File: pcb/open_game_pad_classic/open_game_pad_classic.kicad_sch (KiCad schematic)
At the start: 54 parts, among them J1 COM-09032, J2 COM-09032

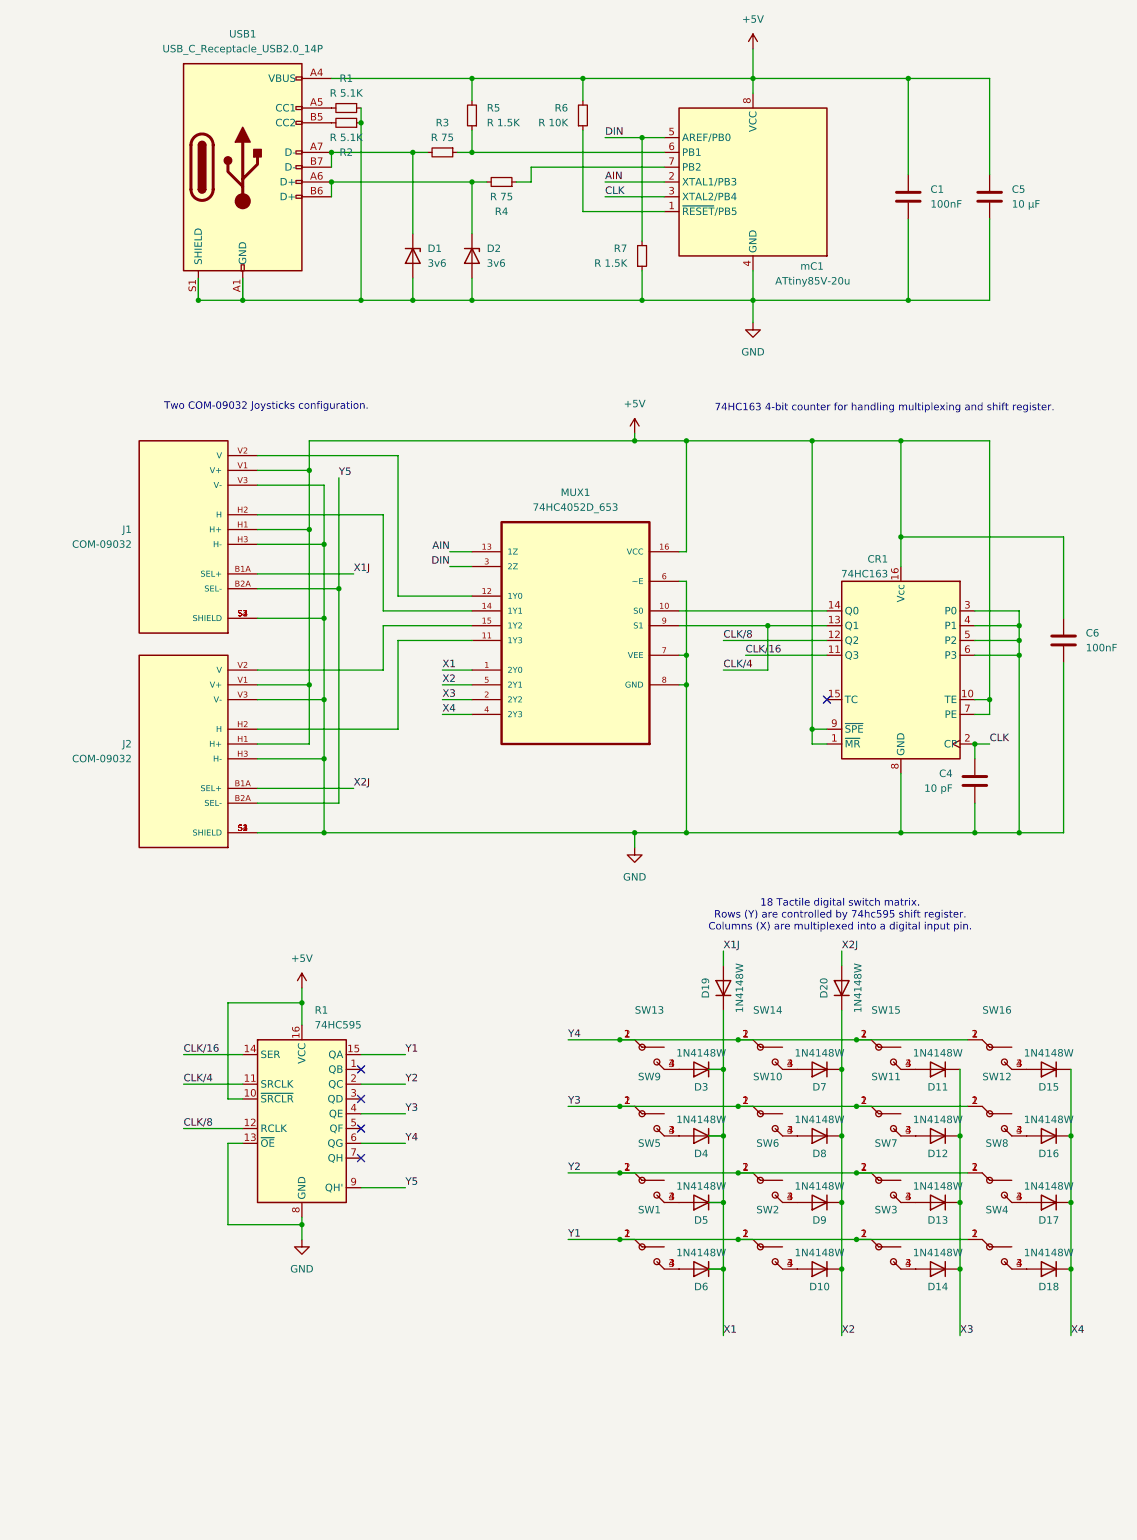
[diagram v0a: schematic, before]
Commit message: Imported footprints.
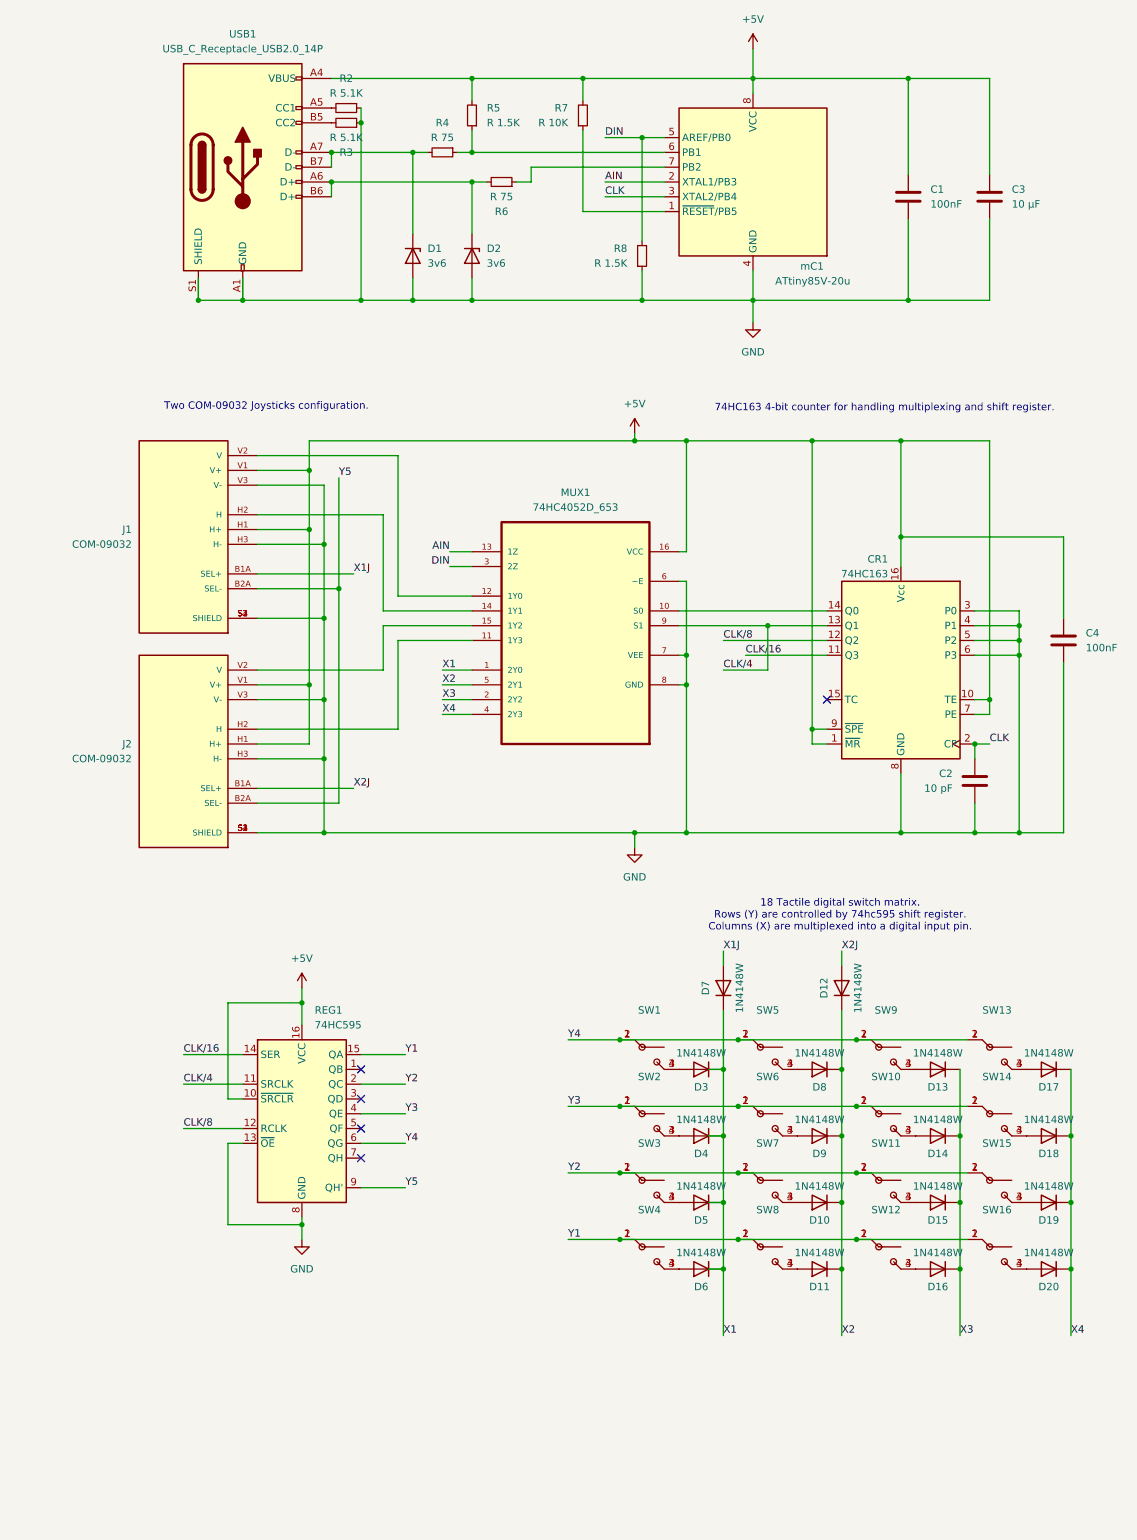
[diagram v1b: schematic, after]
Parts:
- CR1: footprint Package_SO:SOIC-16W_7.5x10.3mm_P1.27mm -> SN74HC163DR:SOIC127P600X175-16N
- REG1: renamed from R1; footprint (none) -> 74HC595DR:SOIC127P600X175-16N
- SW1: renamed from SW13; footprint TS02-66-95-BK-260-LCR-D:SW_TS02-66-95-BK-260-LCR-D -> TS04-66-95-BK-100-SMT:SW_TS04-66-95-BK-100-SMT
- SW10: renamed from SW11; footprint TS02-66-95-BK-260-LCR-D:SW_TS02-66-95-BK-260-LCR-D -> TS04-66-95-BK-100-SMT:SW_TS04-66-95-BK-100-SMT
- SW11: renamed from SW7; footprint TS02-66-95-BK-260-LCR-D:SW_TS02-66-95-BK-260-LCR-D -> TS04-66-95-BK-100-SMT:SW_TS04-66-95-BK-100-SMT
- SW12: renamed from SW3; footprint TS02-66-95-BK-260-LCR-D:SW_TS02-66-95-BK-260-LCR-D -> TS04-66-95-BK-100-SMT:SW_TS04-66-95-BK-100-SMT
- SW13: renamed from SW16; footprint TS02-66-95-BK-260-LCR-D:SW_TS02-66-95-BK-260-LCR-D -> TS04-66-95-BK-100-SMT:SW_TS04-66-95-BK-100-SMT
- SW14: renamed from SW12; footprint TS02-66-95-BK-260-LCR-D:SW_TS02-66-95-BK-260-LCR-D -> TS04-66-95-BK-100-SMT:SW_TS04-66-95-BK-100-SMT
- SW15: renamed from SW8; footprint TS02-66-95-BK-260-LCR-D:SW_TS02-66-95-BK-260-LCR-D -> TS04-66-95-BK-100-SMT:SW_TS04-66-95-BK-100-SMT
- SW16: renamed from SW4; footprint TS02-66-95-BK-260-LCR-D:SW_TS02-66-95-BK-260-LCR-D -> TS04-66-95-BK-100-SMT:SW_TS04-66-95-BK-100-SMT
- SW2: renamed from SW9; footprint TS02-66-95-BK-260-LCR-D:SW_TS02-66-95-BK-260-LCR-D -> TS04-66-95-BK-100-SMT:SW_TS04-66-95-BK-100-SMT
- SW3: renamed from SW5; footprint TS02-66-95-BK-260-LCR-D:SW_TS02-66-95-BK-260-LCR-D -> TS04-66-95-BK-100-SMT:SW_TS04-66-95-BK-100-SMT
- SW4: renamed from SW1; footprint TS02-66-95-BK-260-LCR-D:SW_TS02-66-95-BK-260-LCR-D -> TS04-66-95-BK-100-SMT:SW_TS04-66-95-BK-100-SMT
- SW5: renamed from SW14; footprint TS02-66-95-BK-260-LCR-D:SW_TS02-66-95-BK-260-LCR-D -> TS04-66-95-BK-100-SMT:SW_TS04-66-95-BK-100-SMT
- SW6: renamed from SW10; footprint TS02-66-95-BK-260-LCR-D:SW_TS02-66-95-BK-260-LCR-D -> TS04-66-95-BK-100-SMT:SW_TS04-66-95-BK-100-SMT
- SW7: renamed from SW6; footprint TS02-66-95-BK-260-LCR-D:SW_TS02-66-95-BK-260-LCR-D -> TS04-66-95-BK-100-SMT:SW_TS04-66-95-BK-100-SMT
- SW8: renamed from SW2; footprint TS02-66-95-BK-260-LCR-D:SW_TS02-66-95-BK-260-LCR-D -> TS04-66-95-BK-100-SMT:SW_TS04-66-95-BK-100-SMT
- SW9: renamed from SW15; footprint TS02-66-95-BK-260-LCR-D:SW_TS02-66-95-BK-260-LCR-D -> TS04-66-95-BK-100-SMT:SW_TS04-66-95-BK-100-SMT
- mC1: footprint Package_SO:SOIC-8W_5.3x5.3mm_P1.27mm -> ATTINY85-20SU:SOIC127P798X216-8N
- renumbered C4 to C2, C5 to C3, C6 to C4, D9 to D10, D10 to D11, D20 to D12, D11 to D13, D12 to D14, D13 to D15, D14 to D16, D15 to D17, D16 to D18, D17 to D19, D18 to D20, D19 to D7, D7 to D8, D8 to D9, R1 to R2, R2 to R3, R3 to R4, R4 to R6, R6 to R7, R7 to R8

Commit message: Updated the PCB based on the new schematic design.
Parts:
- C2, C4: footprint Capacitor_SMD:C_0201_0603Metric -> Capacitor_SMD:C_0402_1005Metric
- R7: footprint Resistor_SMD:R_0402_1005Metric -> Resistor_SMD:R_0603_1608Metric
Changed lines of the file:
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@@
 			)
 		)
-		(property "Footprint" "Capacitor_SMD:C_0201_0603Metric"
+		(property "Footprint" "Capacitor_SMD:C_0402_1005Metric"
 			(at 187.6552 130.81 0)
 			(effects
@@
 			)
 		)
-		(property "Footprint" "Resistor_SMD:R_0402_1005Metric"
+		(property "Footprint" "Resistor_SMD:R_0603_1608Metric"
 			(at 104.14 36.83 0)
 			(effects
@@
 			)
 		)
-		(property "Footprint" "Capacitor_SMD:C_0201_0603Metric"
+		(property "Footprint" "Capacitor_SMD:C_0402_1005Metric"
 			(at 170.4848 154.94 0)
 			(effects

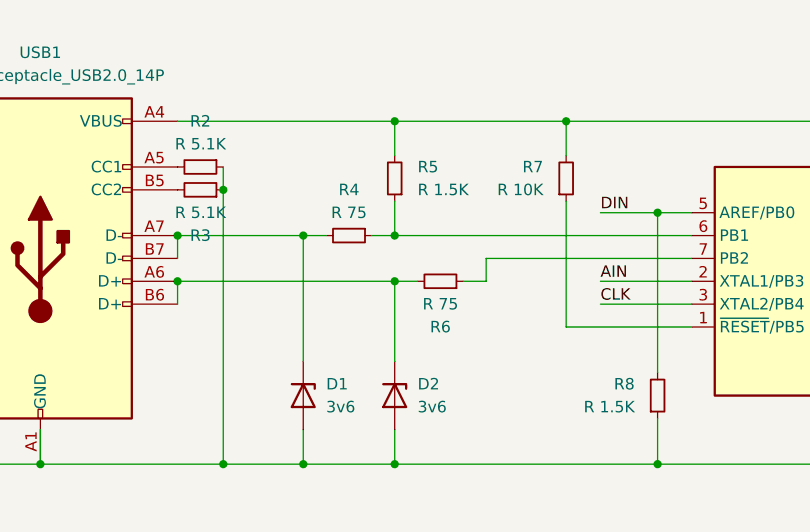
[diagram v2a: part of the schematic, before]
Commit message: Deleted uneccessary files.
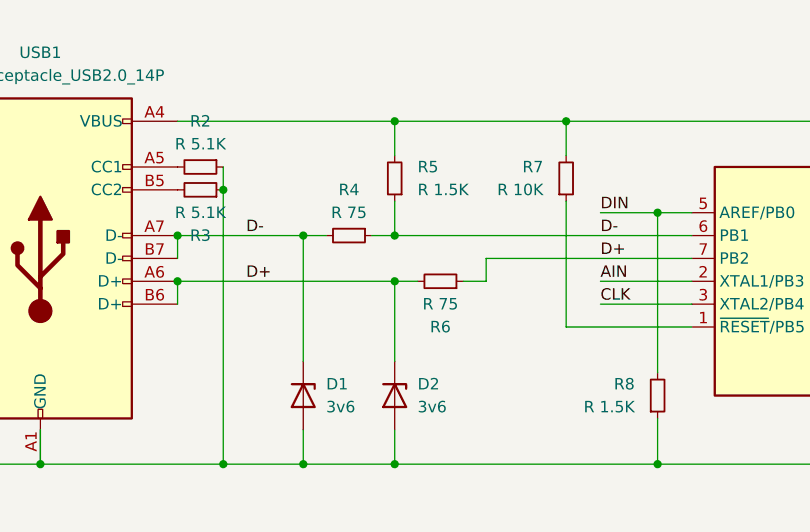
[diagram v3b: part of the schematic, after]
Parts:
- C1, C3: footprint Capacitor_SMD:C_0603_1608Metric -> Capacitor_SMD:C_0402_1005Metric
- D1: footprint Diode_SMD:D_MiniMELF -> Diode_SMD:D_0201_0603Metric
- D2: footprint Diode_SMD:D_MiniMELF -> Diode_SMD:D_0603_1608Metric
- R4, R6: footprint Resistor_SMD:R_0402_1005Metric -> Resistor_SMD:R_0201_0603Metric
- R5: footprint Resistor_SMD:R_0603_1608Metric -> Resistor_SMD:R_0201_0603Metric
- R7, R8: footprint Resistor_SMD:R_0603_1608Metric -> Resistor_SMD:R_0402_1005Metric
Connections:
- net D-: now reaches R4.1, R5.1, mC1.6 (PB1)
- net D-: now also D1.1 (K), R4.2, USB1.A7 (D-), USB1.B7 (D-)
- net D+: now reaches R6.1, mC1.7 (PB2)
- net D+: now also D2.1 (K), R6.2, USB1.A6 (D+), USB1.B6 (D+)
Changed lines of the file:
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@@
 	(wire
 		(pts
-			(xy 60.96 48.26) (xy 85.09 48.26)
-		)
-		(stroke
-			(width 0)
-			(type default)
-		)
-	)
-	(wire
-		(pts
 			(xy 43.18 213.36) (xy 43.18 227.33)
 		)
@@
 	(wire
 		(pts
-			(xy 74.93 43.18) (xy 60.96 43.18)
-		)
-		(stroke
-			(width 0)
-			(type default)
-		)
-	)
-	(wire
-		(pts
 			(xy 80.01 137.16) (xy 85.09 137.16)
 		)
@@
 	(wire
 		(pts
+			(xy 60.96 43.18) (xy 74.93 43.18)
+		)
+		(stroke
+			(width 0)
+			(type default)
+		)
+	)
+	(wire
+		(pts
 			(xy 48.26 132.08) (xy 69.85 132.08)
 		)
@@
 	(wire
 		(pts
+			(xy 60.96 48.26) (xy 85.09 48.26)
+		)
+		(stroke
+			(width 0)
+			(type default)
+		)
+	)
+	(wire
+		(pts
 			(xy 130.81 229.87) (xy 151.13 229.87)
 		)
@@
 		)
 	)
+	(label "D+"
+		(at 68.58 48.26 0)
+		(fields_autoplaced yes)
+		(effects
+			(font
+				(size 1.27 1.27)
+			)
+			(justify left bottom)
+		)
+	)
+	(label "D-"
+		(at 68.58 43.18 0)
+		(fields_autoplaced yes)
+		(effects
+			(font
+				(size 1.27 1.27)
+			)
+			(justify left bottom)
+		)
+	)
 	(label "X1"
 		(at 80.01 132.08 0)
@@
 		)
 	)
+	(label "D+"
+		(at 107.95 45.72 0)
+		(fields_autoplaced yes)
+		(effects
+			(font
+				(size 1.27 1.27)
+			)
+			(justify left bottom)
+		)
+	)
 	(label "X4"
 		(at 80.01 139.7 0)
@@
 		)
 	)
+	(label "D-"
+		(at 107.95 43.18 0)
+		(fields_autoplaced yes)
+		(effects
+			(font
+				(size 1.27 1.27)
+			)
+			(justify left bottom)
+		)
+	)
 	(label "X2"
 		(at 80.01 134.62 0)
@@
 			)
 		)
-		(property "Footprint" "Diode_SMD:D_MiniMELF"
+		(property "Footprint" "Diode_SMD:D_0603_1608Metric"
 			(at 80.645 60.96 0)
 			(effects
@@
 		(on_board yes)
 		(dnp no)
-		(fields_autoplaced yes)
 		(property "Reference" "R4"
 			(at 80.01 38.1 90)
@@
 			)
 		)
-		(property "Footprint" "Resistor_SMD:R_0402_1005Metric"
-			(at 80.01 43.18 0)
+		(property "Footprint" "Resistor_SMD:R_0201_0603Metric"
+			(at 87.376 42.926 0)
 			(effects
 				(font
@@
 			)
 		)
-		(property "Footprint" "Resistor_SMD:R_0603_1608Metric"
+		(property "Footprint" "Resistor_SMD:R_0402_1005Metric"
 			(at 104.14 36.83 0)
 			(effects
@@
 			)
 		)
-		(property "Footprint" "Capacitor_SMD:C_0603_1608Metric"
+		(property "Footprint" "Capacitor_SMD:C_0402_1005Metric"
 			(at 174.9552 54.61 0)
 			(effects
@@
 			)
 		)
-		(property "Footprint" "Diode_SMD:D_MiniMELF"
+		(property "Footprint" "Diode_SMD:D_0201_0603Metric"
 			(at 70.485 60.96 0)
 			(effects
@@
 			)
 		)
-		(property "Footprint" "Resistor_SMD:R_0402_1005Metric"
+		(property "Footprint" "Resistor_SMD:R_0201_0603Metric"
 			(at 90.17 48.26 0)
 			(effects
@@
 			)
 		)
-		(property "Footprint" "Resistor_SMD:R_0603_1608Metric"
+		(property "Footprint" "Resistor_SMD:R_0402_1005Metric"
 			(at 114.3 60.96 0)
 			(effects
@@
 			)
 		)
-		(property "Footprint" "Resistor_SMD:R_0603_1608Metric"
+		(property "Footprint" "Resistor_SMD:R_0201_0603Metric"
 			(at 85.09 36.83 0)
 			(effects
@@
 			)
 		)
-		(property "Footprint" "Capacitor_SMD:C_0603_1608Metric"
+		(property "Footprint" "Capacitor_SMD:C_0402_1005Metric"
 			(at 160.9852 54.61 0)
 			(effects
